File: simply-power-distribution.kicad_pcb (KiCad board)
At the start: 2 copper layers, 0 parts

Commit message: pcb -- layout
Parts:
- added H1: M2.5, MountingHole:MountingHole_2.7mm_M2.5, F.Cu at (67.3, 47.0)
- added H2: M2.5, MountingHole:MountingHole_2.7mm_M2.5, F.Cu at (92.7, 29.2)
- added J1: 55-21 Barrel Jack, Connector_BarrelJack:BarrelJack_Horizontal, F.Cu at (73.3, 36.8)
- added J2: Power distribution, Connector_PinSocket_2.54mm:PinSocket_2x09_P2.54mm_Vertical, F.Cu at (73.7, 45.7)
- added SW1: Power Switch, commons-interconnect_THT:g-switch_22f12-gxxx, F.Cu at (86.7, 36.9)
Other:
- board outline added: 33 x 25.4 mm

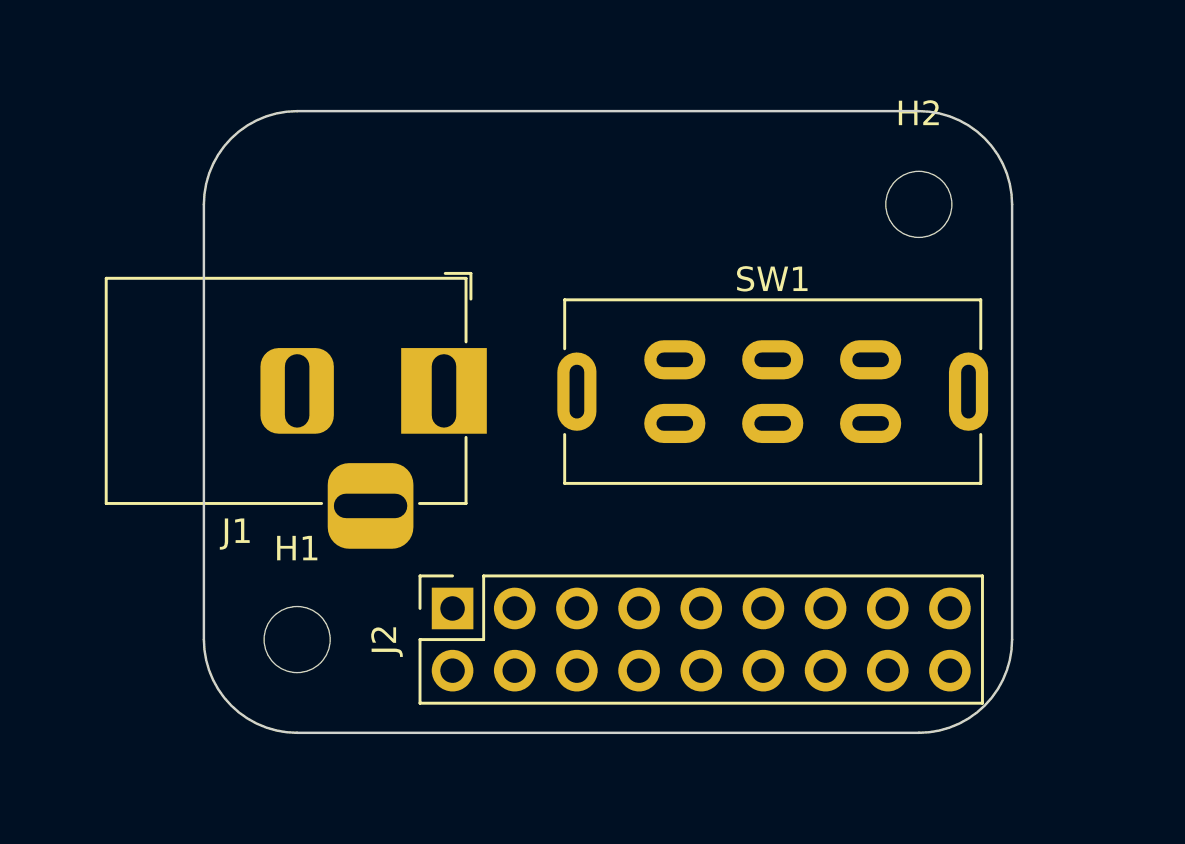
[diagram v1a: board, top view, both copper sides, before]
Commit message: pcb -- traces and markings
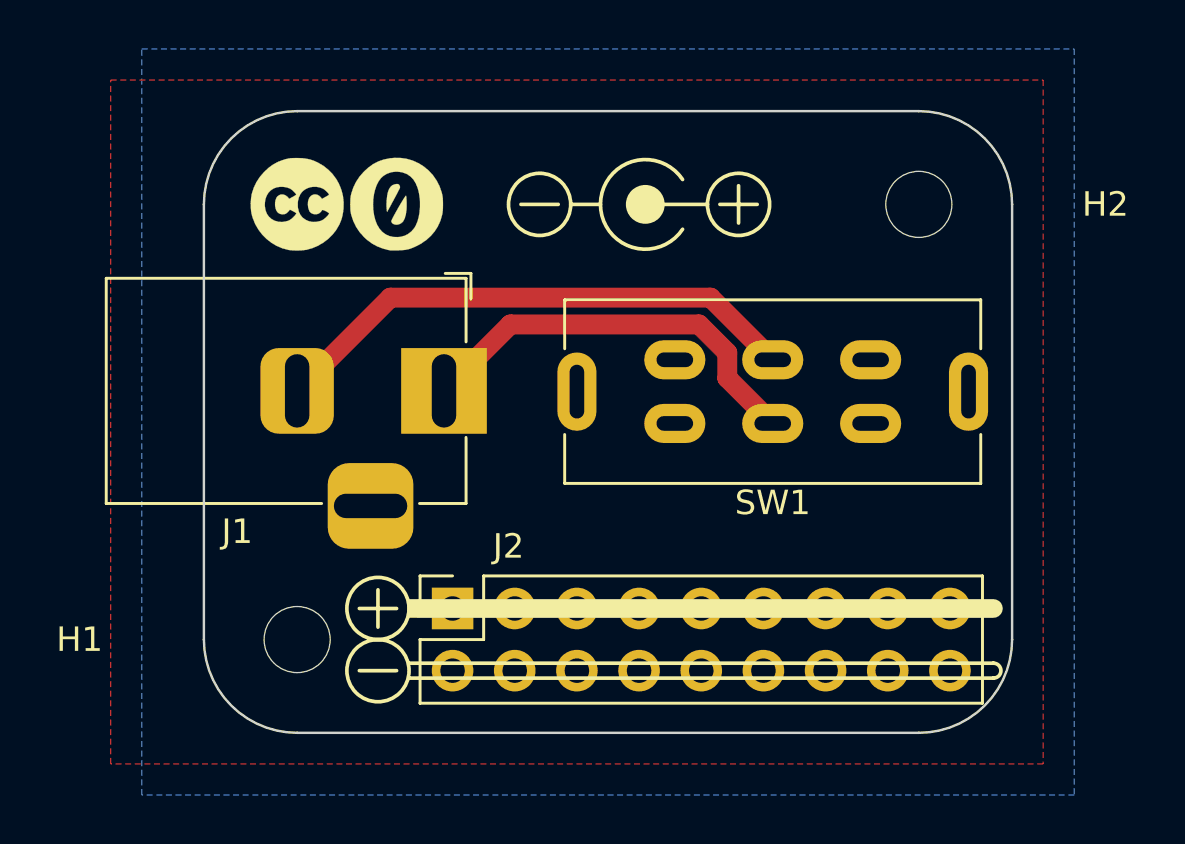
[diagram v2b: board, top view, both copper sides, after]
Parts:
- added G***: LOGO, cliparts:logo--cc--cc, F.Cu at (67.3, 29.2)
- added G***: LOGO, cliparts:logo--cc--zero, F.Cu at (71.4, 29.2)
- added G***: LOGO, cliparts:logo--cc--zero, B.Cu at (67.3, 29.2)
- added G***: LOGO, cliparts:logo--cc--cc, B.Cu at (71.4, 29.2)
- turned SW1 to 180 degrees
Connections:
- J2 pad 1: Net-(J2-Pin_1) -> /VCC
- J2 pad 10: Net-(J2-Pin_10) -> /GND
- J2 pad 11: Net-(J2-Pin_10) -> /VCC
- J2 pad 12: Net-(J2-Pin_10) -> /GND
- J2 pad 13: Net-(J2-Pin_10) -> /VCC
- J2 pad 14: Net-(J2-Pin_10) -> /GND
- J2 pad 15: Net-(J2-Pin_10) -> /VCC
- J2 pad 16: Net-(J2-Pin_10) -> /GND
- J2 pad 17: Net-(J2-Pin_10) -> /VCC
- J2 pad 18: Net-(J2-Pin_10) -> /GND
- J2 pad 2: Net-(J2-Pin_1) -> /GND
- J2 pad 3: Net-(J2-Pin_1) -> /VCC
- J2 pad 4: Net-(J2-Pin_1) -> /GND
- J2 pad 5: Net-(J2-Pin_1) -> /VCC
- J2 pad 6: Net-(J2-Pin_1) -> /GND
- J2 pad 7: Net-(J2-Pin_1) -> /VCC
- J2 pad 8: Net-(J2-Pin_1) -> /GND
- J2 pad 9: Net-(J2-Pin_1) -> /VCC
- SW1 pad 3: Net-(J2-Pin_1) -> /VCC
- SW1 pad 6: Net-(J2-Pin_10) -> /GND
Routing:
- net Net-(J1-Pad2): track 0.00 -> 22.1 mm
- net Net-(J1-Pad1): track 0.00 -> 16.8 mm
- added copper zone on B.Cu, net /GND
- added copper zone on F.Cu, net /VCC
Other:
- board text added: "https://github.com/sporniket/ simply-power-distribution"

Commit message: Prepare RC1
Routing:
- net /VCC: track 0.00 -> 34.2 mm
- added copper zone on F.Cu, net /GND
- removed copper zone on F.Cu, net /VCC
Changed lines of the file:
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@@
   (title_block
     (title "Simply power distribution")
-    (date "2023-12-20")
-    (rev "v0.0.1-DRAFT")
+    (date "2024-01-21")
+    (rev "v0.0.1-RC1")
     (company "Sporniket")
     (comment 4 "Original repository : https://github.com/sporniket/simply-power-distribution")
@@
   (gr_arc (start 79.502 28.194) (mid 82.85762 29.21) (end 79.502 30.226)
     (stroke (width 0.15) (type default)) (layer "B.SilkS"))
-  (gr_rect (start 72.2872 46.0248) (end 71.8808 45.4152)
+  (gr_rect (start 71.8808 45.4152) (end 72.2872 46.0248)
     (stroke (width 0.15) (type solid)) (fill solid) (layer "B.SilkS"))
   (gr_line (start 86.106 29.21) (end 84.582 29.21)
@@
   (segment (start 84.2 33.02) (end 71.12 33.02) (width 0.8128) (layer "F.Cu") (net 2))
   (segment (start 86.74 35.56) (end 84.2 33.02) (width 0.8128) (layer "F.Cu") (net 2))
-  (zone (net 6) (net_name "/VCC") (layer "F.Cu") (hatch edge 0.5)
+  (segment (start 82.296 38.604) (end 82.74 38.16) (width 0.8128) (layer "F.Cu") (net 6))
+  (segment (start 81.788 45.72) (end 82.296 45.212) (width 0.8128) (layer "F.Cu") (net 6))
+  (segment (start 82.296 45.212) (end 82.296 38.604) (width 0.8128) (layer "F.Cu") (net 6))
+  (segment (start 93.98 45.72) (end 83.82 45.72) (width 0.8128) (layer "F.Cu") (net 6))
+  (segment (start 82.74 38.16) (end 83.312 38.732) (width 0.8128) (layer "F.Cu") (net 6))
+  (segment (start 83.312 38.732) (end 83.312 45.212) (width 0.8128) (layer "F.Cu") (net 6))
+  (segment (start 83.312 45.212) (end 83.82 45.72) (width 0.8128) (layer "F.Cu") (net 6))
+  (segment (start 73.66 45.72) (end 81.28 45.72) (width 0.8128) (layer "F.Cu") (net 6))
+  (segment (start 81.28 45.72) (end 81.788 45.72) (width 0.8128) (layer "F.Cu") (net 6))
+  (zone (net 5) (net_name "/GND") (layer "F.Cu") (hatch edge 0.5)
     (connect_pads (clearance 0.5))
     (min_thickness 0.25) (filled_areas_thickness no)
